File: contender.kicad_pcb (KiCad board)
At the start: 2 copper layers, 151 parts, among them SW1 SW_Push, U1 ATmega32U2-AU, U2 PRTR5V0U2X, Y1 16MHz

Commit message: 1.0 finish up
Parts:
- removed CR34, CR35, CR36, CR37, CR38: 0.1u, Capacitor_SMD:C_0603_1608Metric
- removed the D24 at (93.1, 131.0)
- removed L34: YS-SK6812MINI-E, sk6812mini-e:YS-SK6812_backlight
- removed L35, L36, L37, L38: YS-SK6812MINI-E, sk6812mini-e:YS-SK6812_underglow
- removed MX-E-1, MX-E-2, MX-E-3: MX-2U, MX_Only:MXOnly-2U-Hotswap-ReversedStabilizers
- removed the MX24 at (102.1, 58.6)
- added G***: LOGO, contender:contender_logo, B.Cu at (99.9, 68.7)
- added HOLE_M3: VAL**, keyboard_parts:HOLE_M3, F.Cu at (31.1, 126.1)
- added HOLE_M3: VAL**, keyboard_parts:HOLE_M3, F.Cu at (29.0, 46.9)
- added HOLE_M3: VAL**, keyboard_parts:HOLE_M3, F.Cu at (48.1, 27.1)
- added HOLE_M3: VAL**, keyboard_parts:HOLE_M3, F.Cu at (104.1, 27.1)
- added HOLE_M3: VAL**, keyboard_parts:HOLE_M3, F.Cu at (117.5, 141.7)
- C1, C2, C3, C4, C5, C6, CR1, CR10, CR11, CR12, CR13, CR14, CR15, CR16, CR17, CR18, CR19, CR2, CR20, CR21, CR22, CR23, CR24, CR25, CR26, CR27, CR28, CR29, CR3, CR30, CR31, CR32, CR33, CR4, CR5, CR6, CR7, CR8, CR9, D1, D10, D11, D12, D13, D14, D15, D16, D17, D18, D19, D2, D20, D21, D22, D23, D3, D4, D5, D6, D7, D8, D9, F1, R1, R2, R3, R4, R5, R6, SW1, U1, U2, USB1, Y1: moved to B.Cu
- D24: renamed from D25; moved to B.Cu
- D25: renamed from D26; moved to B.Cu
- D26: renamed from D27; moved to B.Cu
- MX20: value MX-1U -> MX-2U; footprint MX_Only:MXOnly-1U-Hotswap -> MX_Only:MXOnly-2U-Hotswap-ReversedStabilizers
- moved U2 176.5 mm to (36.9, 55.3), turned to 180 degrees
- moved L25 176.0 mm to (36.9, 121.5)
- moved D17 173.3 mm to (61.8, 120.5), turned to 90 degrees
- moved C5 171.9 mm to (45.6, 57.6), turned to 180 degrees
- moved C4 171.7 mm to (45.8, 60.8)
- moved L28 171.1 mm to (36.9, 73.4)
- moved CR28 171.0 mm to (29.8, 73.4), turned to 270 degrees
- moved CR24 165.8 mm to (29.8, 102.4), turned to 270 degrees
- moved F1 164.4 mm to (31.5, 59.9), turned to 90 degrees
- moved CR17 162.2 mm to (48.8, 121.4), turned to 270 degrees
- moved C6 158.7 mm to (46.4, 53.4), turned to 90 degrees
- moved D18 158.5 mm to (80.8, 120.5), turned to 90 degrees
- moved Y1 150.7 mm to (54.3, 68.5), turned to 270 degrees
- moved CR27 150.2 mm to (29.8, 83.3), turned to 270 degrees
- moved L22 150.1 mm to (75.0, 140.5)
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- renumbered MX25 to MX24, MX26 to MX25, MX27 to MX26
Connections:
- L29 pad 1: Net-(L29-Pad1) -> +5V
- L30 pad 1: Net-(L30-Pad1) -> +5V
- U1 pad 10: COL0 -> ROWFN
- U1 pad 11: COL1 -> Net-(U1-Pad11)
- U1 pad 12: ROW2 -> COL1
- U1 pad 13: ROW3 -> Net-(R6-Pad2)
- U1 pad 14: Net-(U1-Pad14) -> COL3
- U1 pad 15: Net-(U1-Pad15) -> COL4
- U1 pad 16: COL3 -> ROW4
- U1 pad 18: Net-(U1-Pad18) -> ROW3
- U1 pad 19: COL4 -> ROW1
- U1 pad 20: ROW4 -> Net-(U1-Pad20)
- U1 pad 21: Net-(U1-Pad21) -> ROW2
- U1 pad 22: Net-(U1-Pad22) -> COL0
- U1 pad 23: ROWFN -> RGBLED
- U1 pad 25: ROW1 -> Net-(U1-Pad25)
- U1 pad 26: ROW0 -> Net-(U1-Pad26)
- U1 pad 7: Net-(R6-Pad2) -> Net-(U1-Pad7)
- U1 pad 9: Net-(U1-Pad9) -> ROW0
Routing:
- net GND: track 0.00 -> 946.6 mm, vias 0 -> 54
- net +5V: track 0.00 -> 885.0 mm, vias 0 -> 75
- net COL1: track 0.00 -> 213.5 mm, vias 0 -> 4
- net ROW3: track 0.00 -> 189.4 mm, vias 0 -> 8
- net COL4: track 0.00 -> 188.7 mm, vias 0 -> 2
- net COL3: track 0.00 -> 184.7 mm, vias 0 -> 4
- net Net-(L23-Pad2): track 0.00 -> 162.4 mm, vias 0 -> 4
- net ROWFN: track 0.00 -> 161.3 mm, vias 0 -> 8
- net COL2: track 0.00 -> 157.9 mm, vias 0 -> 4
- net ROW2: track 0.00 -> 148.4 mm, vias 0 -> 8
- net ROW4: track 0.00 -> 138.1 mm, vias 0 -> 6
- net ROW1: track 0.00 -> 123.2 mm, vias 0 -> 7
- net Net-(L20-Pad2): track 0.00 -> 101.6 mm, vias 0 -> 4
- net Net-(L4-Pad2): track 0.00 -> 95.5 mm, vias 0 -> 2
- net Net-(L16-Pad2): track 0.00 -> 91.7 mm, vias 0 -> 2
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- added copper zone on B.Cu, net GND
- added copper zone on F.Cu, net GND
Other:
- board outline added: 97.8 x 121.5 mm
- net class Default: trace_width 0.25 -> 0.254; via_dia 0.8 -> 0.6
- net class Power added: clearance 0.2, trace_width 0.381, via_dia 0.8, via_drill 0.4
- rule pad_to_mask_clearance: 0 -> 0.1
- board text added: "designed by stupa.dev"

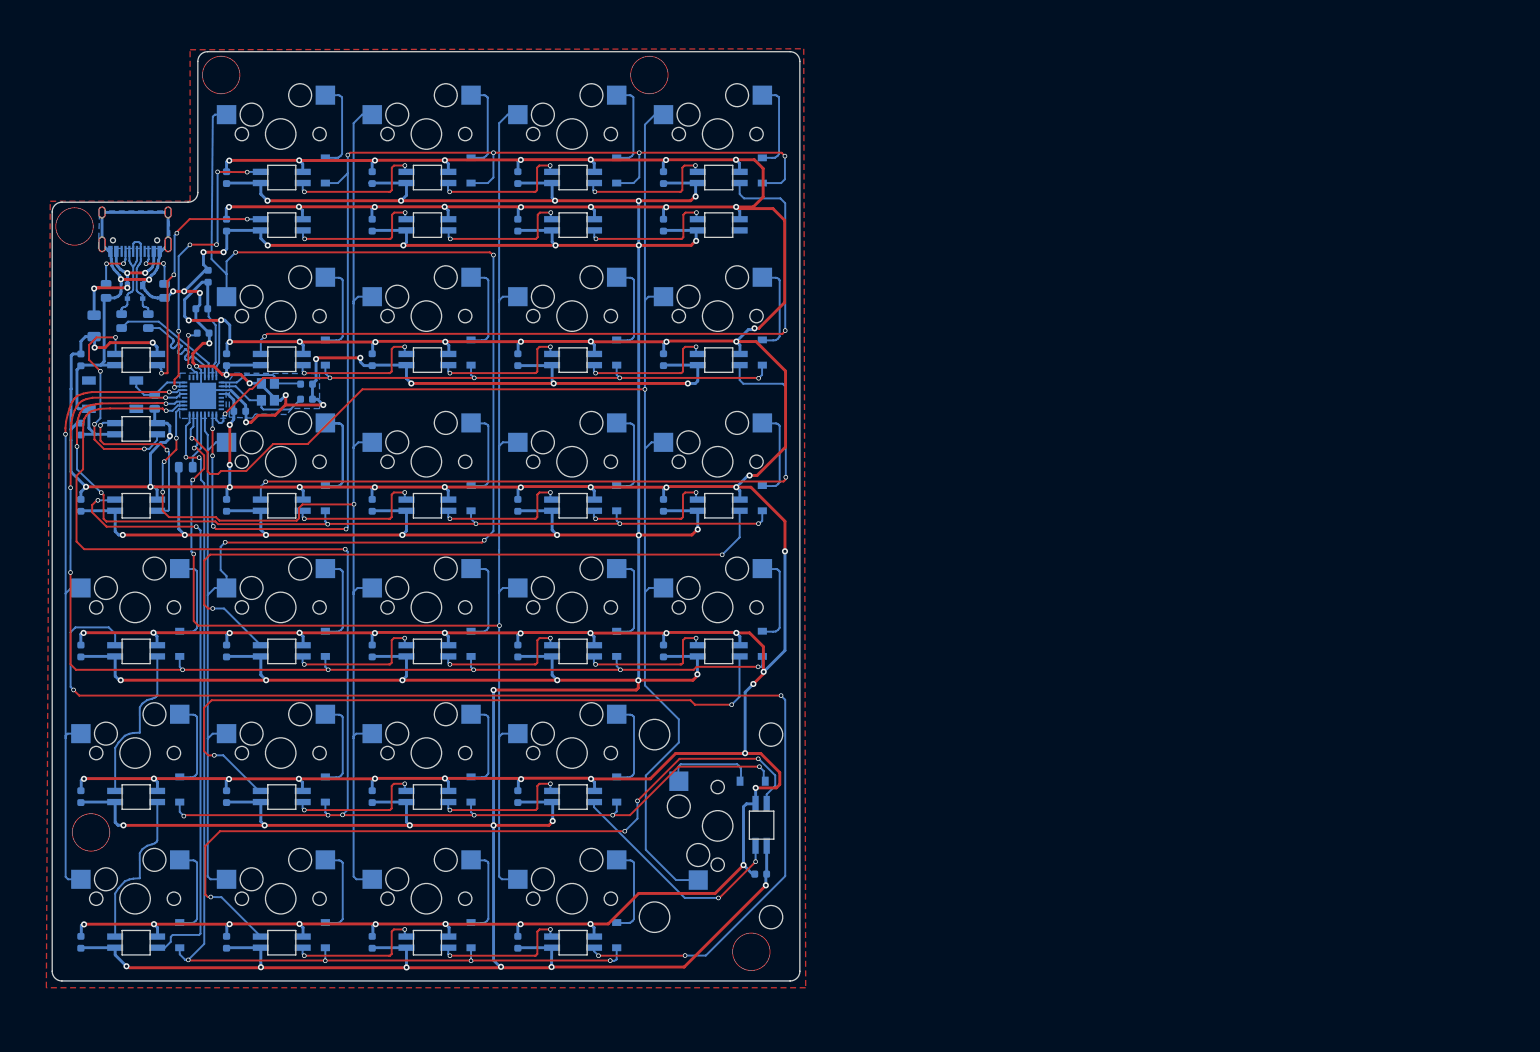
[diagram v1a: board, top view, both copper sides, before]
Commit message: fix mounthole point
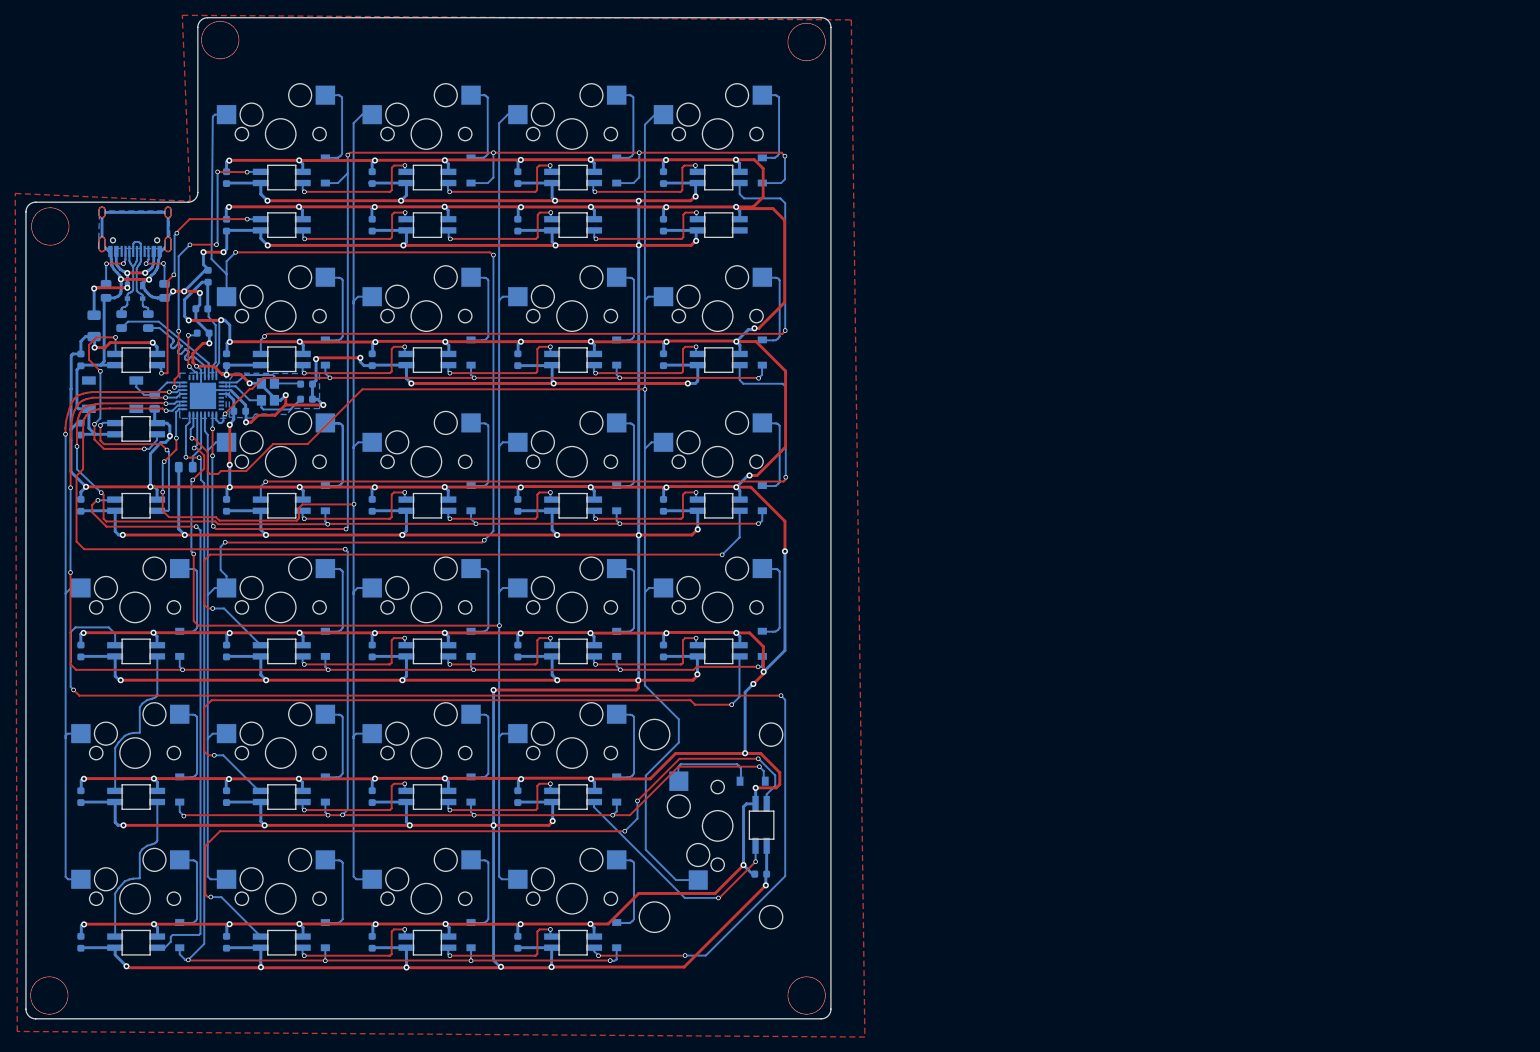
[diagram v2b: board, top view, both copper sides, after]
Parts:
- removed the HOLE_M3 at (31.1, 126.1)
- removed the HOLE_M3 at (117.5, 141.7)
- added HOLE_M3: VAL**, keyboard_parts:HOLE_M3, F.Cu at (25.7, 147.4)
- added HOLE_M3: VAL**, keyboard_parts:HOLE_M3, F.Cu at (124.7, 147.4)
- moved HOLE_M3 21.0 mm to (124.7, 22.7)
- moved HOLE_M3 4.57 mm to (48.0, 22.5)
- moved HOLE_M3 3.18 mm to (25.8, 46.9)
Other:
- board size 97.8 x 121.5 mm -> 105.3 x 130.9 mm
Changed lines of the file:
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@@
   )
   (module keyboard_parts:HOLE_M3 (layer F.Cu)
-    (at 31.115 126.111)
+    (at 25.654 147.447)
     (fp_text reference HOLE_M3 (at 0 -4.5) (layer F.SilkS) hide
       (effects (font (size 1.524 1.524) (thickness 0.3048)))
@@
   )
   (module keyboard_parts:HOLE_M3 (layer F.Cu)
-    (at 28.956 46.863)
+    (at 25.781 46.863)
     (fp_text reference HOLE_M3 (at 0 -4.5) (layer F.SilkS) hide
       (effects (font (size 1.524 1.524) (thickness 0.3048)))
@@
   )
   (module keyboard_parts:HOLE_M3 (layer F.Cu)
-    (at 48.133 27.051)
+    (at 48.006 22.479)
     (fp_text reference HOLE_M3 (at 0 -4.5) (layer F.SilkS) hide
       (effects (font (size 1.524 1.524) (thickness 0.3048)))
@@
   )
   (module keyboard_parts:HOLE_M3 (layer F.Cu)
-    (at 104.14 27.051)
+    (at 124.714 22.733)
     (fp_text reference HOLE_M3 (at 0 -4.5) (layer F.SilkS) hide
       (effects (font (size 1.524 1.524) (thickness 0.3048)))
@@
   )
   (module keyboard_parts:HOLE_M3 (layer F.Cu)
-    (at 117.475 141.732)
+    (at 124.714 147.447)
     (fp_text reference HOLE_M3 (at 0 -4.5) (layer F.SilkS) hide
       (effects (font (size 1.524 1.524) (thickness 0.3048)))
@@
     )
   )
-  (gr_text "designed by stupa.dev" (at 82.55 69.469) (layer B.SilkS)
-    (effects (font (size 0.75 0.75) (thickness 0.125)) (justify mirror))
-  )
-  (dimension 124.333584 (width 0.12) (layer Dwgs.User)
-    (gr_text "124.334 mm" (at 20.461355 85.543213 270.1755739) (layer Dwgs.User)
+  (dimension 130.950242 (width 0.12) (layer Dwgs.User)
+    (gr_text "130.950 mm" (at 129.349495 85.016586 -89.83329758) (layer Dwgs.User)
       (effects (font (size 1 1) (thickness 0.15)))
     )
-    (feature1 (pts (xy 23.495 147.701) (xy 21.335431 147.707618)))
-    (feature2 (pts (xy 23.114 23.368) (xy 20.954431 23.374618)))
-    (crossbar (pts (xy 21.540849 23.372821) (xy 21.921849 147.705821)))
-    (arrow1a (pts (xy 21.921849 147.705821) (xy 21.331979 146.58112)))
-    (arrow1b (pts (xy 21.921849 147.705821) (xy 22.504815 146.577526)))
-    (arrow2a (pts (xy 21.540849 23.372821) (xy 20.957883 24.501116)))
-    (arrow2b (pts (xy 21.540849 23.372821) (xy 22.130719 24.497522)))
-  )
-  (dimension 99.569296 (width 0.12) (layer Dwgs.User)
-    (gr_text "99.569 mm" (at 74.784897 148.836147 359.7076771) (layer Dwgs.User)
-      (effects (font (size 1 1) (thickness 0.15)))
-    )
-    (feature1 (pts (xy 125.222 21.082) (xy 124.572385 148.406578)))
-    (feature2 (pts (xy 25.654 20.574) (xy 25.004385 147.898578)))
-    (crossbar (pts (xy 25.007377 147.312164) (xy 124.575377 147.820164)))
-    (arrow1a (pts (xy 124.575377 147.820164) (xy 123.445896 148.40083)))
-    (arrow1b (pts (xy 124.575377 147.820164) (xy 123.45188 147.228004)))
-    (arrow2a (pts (xy 25.007377 147.312164) (xy 26.130874 147.904324)))
-    (arrow2b (pts (xy 25.007377 147.312164) (xy 26.136858 146.731498)))
+    (feature1 (pts (xy 123.571005 19.558) (xy 128.475418 19.543731)))
+    (feature2 (pts (xy 123.952005 150.507688) (xy 128.856418 150.493419)))
+    (crossbar (pts (xy 128.27 150.495125) (xy 127.889 19.545437)))
+    (arrow1a (pts (xy 127.889 19.545437) (xy 128.478696 20.67023)))
+    (arrow1b (pts (xy 127.889 19.545437) (xy 127.305859 20.673642)))
+    (arrow2a (pts (xy 128.27 150.495125) (xy 128.853141 149.36692)))
+    (arrow2b (pts (xy 128.27 150.495125) (xy 127.680304 149.370332)))
+  )
+  (dimension 100.584 (width 0.12) (layer Dwgs.User)
+    (gr_text "100.584 mm" (at 73.533 155.843298) (layer Dwgs.User)
+      (effects (font (size 1 1) (thickness 0.15)))
+    )
+    (feature1 (pts (xy 23.241 145.542) (xy 23.241 155.159719)))
+    (feature2 (pts (xy 123.825 145.542) (xy 123.825 155.159719)))
+    (crossbar (pts (xy 123.825 154.573298) (xy 23.241 154.573298)))
+    (arrow1a (pts (xy 23.241 154.573298) (xy 24.367504 153.986877)))
+    (arrow1b (pts (xy 23.241 154.573298) (xy 24.367504 155.159719)))
+    (arrow2a (pts (xy 123.825 154.573298) (xy 122.698496 153.986877)))
+    (arrow2b (pts (xy 123.825 154.573298) (xy 122.698496 155.159719)))
+  )
+  (gr_text "designed by stupa.dev" (at 82.55 69.469) (layer B.SilkS)
+    (effects (font (size 0.75 0.75) (thickness 0.125)) (justify mirror))
   )
   (gr_line (start 120.421 123.33) (end 117.221 123.33) (layer Edge.Cuts) (width 0.05))
@@
   (gr_line (start 54.229 38.862) (end 57.899 38.862) (layer Edge.Cuts) (width 0.05))
   (gr_arc (start 43.815 42.418) (end 43.815 43.688) (angle -90) (layer Edge.Cuts) (width 0.05))
-  (gr_arc (start 46.355 25.273) (end 46.355 24.003) (angle -90) (layer Edge.Cuts) (width 0.05))
-  (gr_arc (start 27.305 44.958) (end 27.305 43.688) (angle -90) (layer Edge.Cuts) (width 0.05))
-  (gr_arc (start 27.305 144.272) (end 26.035 144.272) (angle -90) (layer Edge.Cuts) (width 0.05))
-  (gr_arc (start 122.555 144.272) (end 122.555 145.542) (angle -90) (layer Edge.Cuts) (width 0.05))
-  (gr_arc (start 122.555 25.273) (end 123.825 25.273) (angle -90) (layer Edge.Cuts) (width 0.05))
-  (gr_line (start 43.815 43.688) (end 27.305 43.688) (layer Edge.Cuts) (width 0.05))
-  (gr_line (start 45.085 25.273) (end 45.085 42.418) (layer Edge.Cuts) (width 0.05))
-  (gr_line (start 46.355 24.003) (end 122.555 24.003) (layer Edge.Cuts) (width 0.05))
-  (gr_line (start 27.305 145.542) (end 122.555 145.542) (layer Edge.Cuts) (width 0.05))
-  (gr_line (start 26.035 44.958) (end 26.035 144.272) (layer Edge.Cuts) (width 0.05))
-  (gr_line (start 123.825 144.272) (end 123.825 25.273) (layer Edge.Cuts) (width 0.05))
+  (gr_arc (start 46.355 20.828) (end 46.355 19.558) (angle -90) (layer Edge.Cuts) (width 0.05))
+  (gr_arc (start 23.876 44.958) (end 23.876 43.688) (angle -90) (layer Edge.Cuts) (width 0.05))
+  (gr_arc (start 23.876 149.225) (end 22.606 149.225) (angle -90) (layer Edge.Cuts) (width 0.05))
+  (gr_arc (start 126.619 149.225) (end 126.619 150.495) (angle -90) (layer Edge.Cuts) (width 0.05))
+  (gr_arc (start 126.619 20.828) (end 127.889 20.828) (angle -90) (layer Edge.Cuts) (width 0.05))
+  (gr_line (start 43.815 43.688) (end 23.876 43.688) (layer Edge.Cuts) (width 0.05))
+  (gr_line (start 45.085 20.828) (end 45.085 42.418) (layer Edge.Cuts) (width 0.05))
+  (gr_line (start 46.355 19.558) (end 126.619 19.558) (layer Edge.Cuts) (width 0.05))
+  (gr_line (start 23.876 150.495) (end 126.619 150.495) (layer Edge.Cuts) (width 0.05))
+  (gr_line (start 22.606 44.958) (end 22.606 149.225) (layer Edge.Cuts) (width 0.05))
+  (gr_line (start 127.889 149.225) (end 127.889 20.828) (layer Edge.Cuts) (width 0.05))
   (segment (start 47.93996 68.25996) (end 47.29988 68.25996) (width 0.254) (layer B.Cu) (net 0))
   (segment (start 45.50664 66.71056) (end 45.50664 67.54368) (width 0.254) (layer B.Cu) (net 0))
@@
     (polygon
       (pts
-        (xy 124.587 146.431) (xy 25.273 146.431) (xy 25.781 43.561) (xy 44.069 43.561) (xy 44.069 23.749)
-        (xy 124.333 23.622)
+        (xy 132.334 152.87625) (xy 21.463 152.146) (xy 21.209 42.545) (xy 44.069 43.561) (xy 43.053 19.2405)
+        (xy 130.556 19.84375)
       )
     )
